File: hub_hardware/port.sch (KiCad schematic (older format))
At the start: 13 parts, among them P1 CONN_4, U4 ISL83485IBZ, U5 2CH-TVS

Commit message: kicad hardware files
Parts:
- C7: value C -> 100n; footprint ~ -> SA0603
- D3, D4: footprint (none) -> SA0603_LED
- P1: footprint (none) -> Assman-6p4c
- R10: footprint (none) -> C2
- R11: value 2K2 -> 10K; footprint (none) -> SA0603
- R43, R6, R7, R8, R9: footprint (none) -> SA0603
- U4: footprint (none) -> SO8E
- U5: footprint (none) -> SOT23
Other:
- note added: "PTC optional"

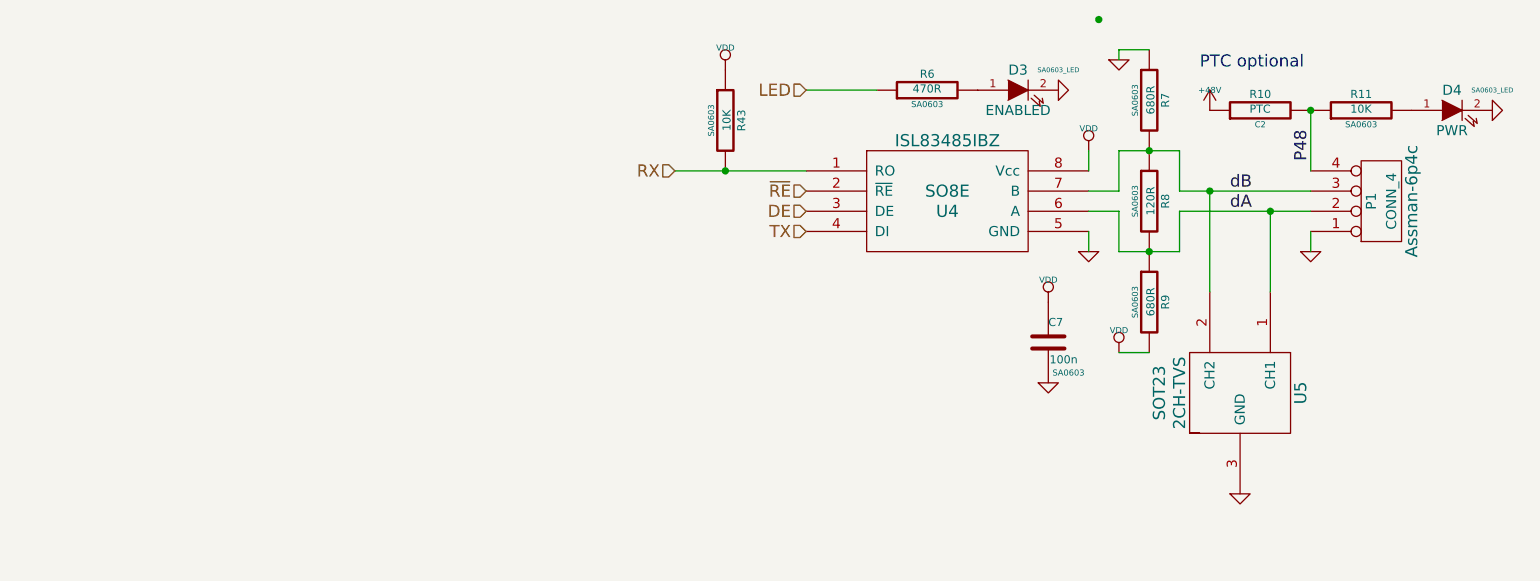
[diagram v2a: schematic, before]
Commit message: Copper for the hub
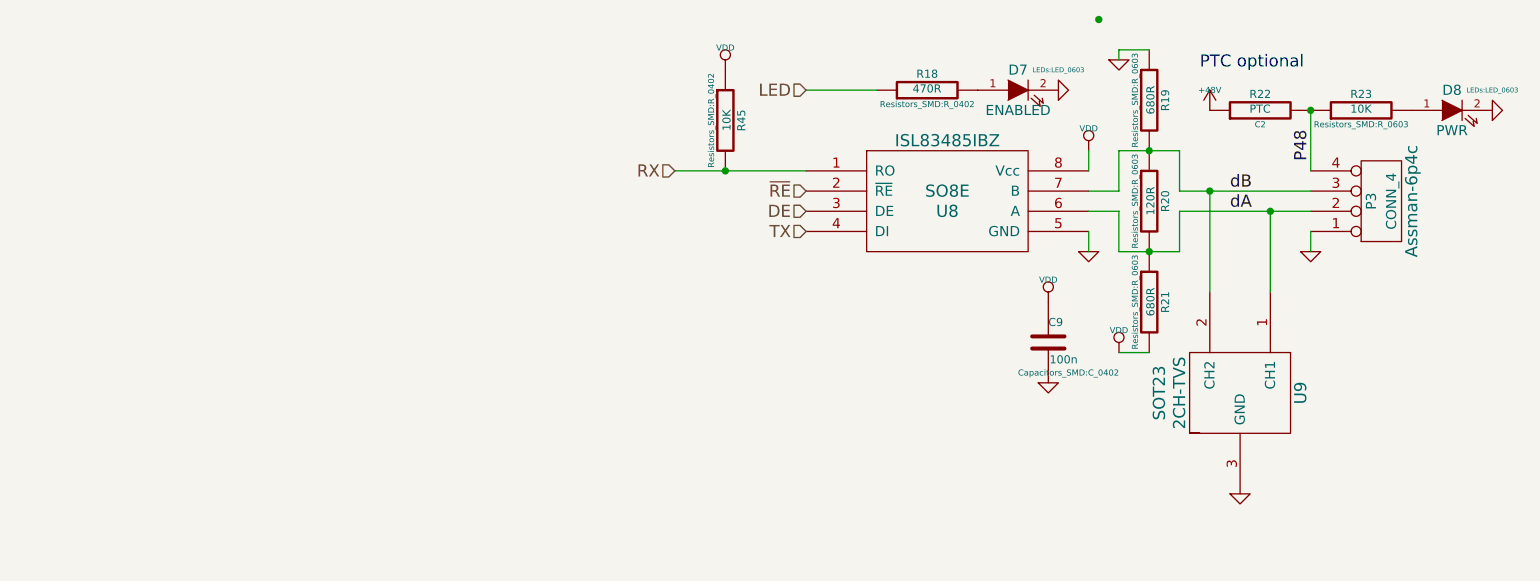
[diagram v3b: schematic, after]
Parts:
- C7: footprint SA0603 -> Capacitors_SMD:C_0402
- D3, D4: footprint SA0603_LED -> LEDs:LED_0603
- R11, R7, R8, R9: footprint SA0603 -> Resistors_SMD:R_0603
- R43, R6: footprint SA0603 -> Resistors_SMD:R_0402
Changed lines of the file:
@@
 AR Path="/556BE805/556BC9D7" Ref="P5"  Part="1"
 AR Path="/556BE816/556BC9D7" Ref="P6"  Part="1"
-F 0 "P1" V 7700 3700 50  0000 C CNN
+F 0 "P3" V 7700 3700 50  0000 C CNN
 F 1 "CONN_4" V 7800 3700 50  0000 C CNN
 F 2 "Assman-6p4c" V 7900 3700 60  0000 C CNN
@@
 AR Path="/556BE816/556BC9DD" Ref="R38"  Part="1"
 AR Path="/556BC9DD" Ref="R38"  Part="1"
-F 0 "R8" V 6680 3700 40  0000 C CNN
+F 0 "R20" V 6680 3700 40  0000 C CNN
 F 1 "120R" V 6607 3701 40  0000 C CNN
-F 2 "SA0603" V 6530 3700 30  0000 C CNN
+F 2 "Resistors_SMD:R_0603" V 6530 3700 30  0000 C CNN
 F 3 "" H 6600 3700 30  0000 C CNN
 	1    6600 3700
@@
 AR Path="/556BE805/556BC9EF" Ref="U12"  Part="1"
 AR Path="/556BE816/556BC9EF" Ref="U14"  Part="1"
-F 0 "U4" H 5600 3650 60  0000 C CNN
+F 0 "U8" H 5600 3650 60  0000 C CNN
 F 1 "ISL83485IBZ" H 5600 4000 60  0000 C CNN
 F 2 "SO8E" H 5600 3750 60  0000 C CNN
@@
 AR Path="/556BE805/556BCB2D" Ref="U13"  Part="1"
 AR Path="/556BE816/556BCB2D" Ref="U15"  Part="1"
-F 0 "U5" H 7050 4950 60  0000 C CNN
+F 0 "U9" H 7050 4950 60  0000 C CNN
 F 1 "2CH-TVS" H 7050 4350 60  0000 C CNN
 F 2 "SOT23" H 7050 4250 60  0000 C CNN
@@
 AR Path="/556BE816/556BCC86" Ref="R40"  Part="1"
 AR Path="/556BCC86" Ref="R40"  Part="1"
-F 0 "R10" V 7230 3250 40  0000 C CNN
+F 0 "R22" V 7230 3250 40  0000 C CNN
 F 1 "PTC" V 7157 3251 40  0000 C CNN
 F 2 "C2" V 7080 3250 30  0000 C CNN
@@
 AR Path="/556BE816/556BCD66" Ref="R41"  Part="1"
 AR Path="/556BCD66" Ref="R41"  Part="1"
-F 0 "R11" V 7730 3250 40  0000 C CNN
+F 0 "R23" V 7730 3250 40  0000 C CNN
 F 1 "10K" V 7657 3251 40  0000 C CNN
-F 2 "SA0603" V 7580 3250 30  0000 C CNN
+F 2 "Resistors_SMD:R_0603" V 7580 3250 30  0000 C CNN
 F 3 "" H 7650 3250 30  0000 C CNN
 	1    7650 3250
@@
 AR Path="/556BE816/556BCD84" Ref="D14"  Part="1"
 AR Path="/556BCD84" Ref="D14"  Part="1"
-F 0 "D4" H 8100 3350 50  0000 C CNN
+F 0 "D8" H 8100 3350 50  0000 C CNN
 F 1 "PWR" H 8100 3150 50  0000 C CNN
-F 2 "SA0603_LED" H 8300 3350 24  0000 C CNN
+F 2 "LEDs:LED_0603" H 8300 3350 24  0000 C CNN
 F 3 "" H 8100 3250 60  0000 C CNN
 	1    8100 3250
@@
 AR Path="/556BE816/556BCEEE" Ref="R36"  Part="1"
 AR Path="/556BCEEE" Ref="R36"  Part="1"
-F 0 "R6" V 5580 3150 40  0000 C CNN
+F 0 "R18" V 5580 3150 40  0000 C CNN
 F 1 "470R" V 5507 3151 40  0000 C CNN
-F 2 "SA0603" V 5430 3150 30  0000 C CNN
+F 2 "Resistors_SMD:R_0402" V 5430 3150 30  0000 C CNN
 F 3 "" H 5500 3150 30  0000 C CNN
 	1    5500 3150
@@
 AR Path="/556BE816/556BCEFD" Ref="D13"  Part="1"
 AR Path="/556BCEFD" Ref="D13"  Part="1"
-F 0 "D3" H 5950 3250 50  0000 C CNN
+F 0 "D7" H 5950 3250 50  0000 C CNN
 F 1 "ENABLED" H 5950 3050 50  0000 C CNN
-F 2 "SA0603_LED" H 6150 3250 24  0000 C CNN
+F 2 "LEDs:LED_0603" H 6150 3250 24  0000 C CNN
 F 3 "" H 5950 3150 60  0000 C CNN
 	1    5950 3150
@@
 AR Path="/556BE816/556BD0FA" Ref="R39"  Part="1"
 AR Path="/556BD0FA" Ref="R39"  Part="1"
-F 0 "R9" V 6680 4200 40  0000 C CNN
+F 0 "R21" V 6680 4200 40  0000 C CNN
 F 1 "680R" V 6607 4201 40  0000 C CNN
-F 2 "SA0603" V 6530 4200 30  0000 C CNN
+F 2 "Resistors_SMD:R_0603" V 6530 4200 30  0000 C CNN
 F 3 "" H 6600 4200 30  0000 C CNN
 	1    6600 4200
@@
 AR Path="/556BE816/556BD4F2" Ref="R37"  Part="1"
 AR Path="/556BD4F2" Ref="R37"  Part="1"
-F 0 "R7" V 6680 3200 40  0000 C CNN
+F 0 "R19" V 6680 3200 40  0000 C CNN
 F 1 "680R" V 6607 3201 40  0000 C CNN
-F 2 "SA0603" V 6530 3200 30  0000 C CNN
+F 2 "Resistors_SMD:R_0603" V 6530 3200 30  0000 C CNN
 F 3 "" H 6600 3200 30  0000 C CNN
 	1    6600 3200
@@
 AR Path="/556BE816/556BE2B4" Ref="R48"  Part="1"
 AR Path="/556BE2B4" Ref="R48"  Part="1"
-F 0 "R43" V 4580 3300 40  0000 C CNN
+F 0 "R45" V 4580 3300 40  0000 C CNN
 F 1 "10K" V 4507 3301 40  0000 C CNN
-F 2 "SA0603" V 4430 3300 30  0000 C CNN
+F 2 "Resistors_SMD:R_0402" V 4430 3300 30  0000 C CNN
 F 3 "" H 4500 3300 30  0000 C CNN
 	1    4500 3300
@@
 AR Path="/556BE816/556C536A" Ref="C12"  Part="1"
 AR Path="/556C536A" Ref="C12"  Part="1"
-F 0 "C7" H 6100 4500 40  0000 L CNN
+F 0 "C9" H 6100 4500 40  0000 L CNN
 F 1 "100n" H 6106 4315 40  0000 L CNN
-F 2 "SA0603" H 6200 4250 30  0000 C CNN
+F 2 "Capacitors_SMD:C_0402" H 6200 4250 30  0000 C CNN
 F 3 "~" H 6100 4400 60  0000 C CNN
 	1    6100 4400

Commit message: Hub gerbers; Reverting changes to lux API;
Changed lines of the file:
@@
 AR Path="/556BE805/556BC9D7" Ref="P5"  Part="1"
 AR Path="/556BE816/556BC9D7" Ref="P6"  Part="1"
-F 0 "P3" V 7700 3700 50  0000 C CNN
+F 0 "P1" V 7700 3700 50  0000 C CNN
 F 1 "CONN_4" V 7800 3700 50  0000 C CNN
 F 2 "Assman-6p4c" V 7900 3700 60  0000 C CNN
@@
 AR Path="/556BE816/556BC9DD" Ref="R38"  Part="1"
 AR Path="/556BC9DD" Ref="R38"  Part="1"
-F 0 "R20" V 6680 3700 40  0000 C CNN
+F 0 "R8" V 6680 3700 40  0000 C CNN
 F 1 "120R" V 6607 3701 40  0000 C CNN
 F 2 "Resistors_SMD:R_0603" V 6530 3700 30  0000 C CNN
@@
 AR Path="/556BE816/556BC9E3" Ref="#PWR099"  Part="1"
 AR Path="/556BC9E3" Ref="#PWR098"  Part="1"
-F 0 "#PWR099" H 7400 3950 30  0001 C CNN
+F 0 "#PWR039" H 7400 3950 30  0001 C CNN
 F 1 "GND" H 7400 3880 30  0001 C CNN
 F 2 "" H 7400 3950 60  0000 C CNN
@@
 AR Path="/556BE805/556BC9E9" Ref="#PWR088"  Part="1"
 AR Path="/556BE816/556BC9E9" Ref="#PWR0100"  Part="1"
-F 0 "#PWR0100" H 6900 3380 20  0001 C CNN
+F 0 "#PWR040" H 6900 3380 20  0001 C CNN
 F 1 "+48V" H 6900 3350 30  0000 C CNN
 F 2 "" H 6900 3250 60  0000 C CNN
@@
 AR Path="/556BE805/556BC9EF" Ref="U12"  Part="1"
 AR Path="/556BE816/556BC9EF" Ref="U14"  Part="1"
-F 0 "U8" H 5600 3650 60  0000 C CNN
+F 0 "U4" H 5600 3650 60  0000 C CNN
 F 1 "ISL83485IBZ" H 5600 4000 60  0000 C CNN
 F 2 "SO8E" H 5600 3750 60  0000 C CNN
@@
 AR Path="/556BE816/556BC9F5" Ref="#PWR0101"  Part="1"
 AR Path="/556BC9F5" Ref="#PWR0100"  Part="1"
-F 0 "#PWR0101" H 6300 3950 30  0001 C CNN
+F 0 "#PWR041" H 6300 3950 30  0001 C CNN
 F 1 "GND" H 6300 3880 30  0001 C CNN
 F 2 "" H 6300 3950 60  0000 C CNN
@@
 AR Path="/556BE805/556BCABF" Ref="#PWR090"  Part="1"
 AR Path="/556BE816/556BCABF" Ref="#PWR0102"  Part="1"
-F 0 "#PWR0102" H 6300 3550 30  0001 C CNN
+F 0 "#PWR042" H 6300 3550 30  0001 C CNN
 F 1 "VDD" H 6300 3560 30  0000 C CNN
 F 2 "" H 6300 3450 60  0000 C CNN
@@
 AR Path="/556BE805/556BCB2D" Ref="U13"  Part="1"
 AR Path="/556BE816/556BCB2D" Ref="U15"  Part="1"
-F 0 "U9" H 7050 4950 60  0000 C CNN
+F 0 "U5" H 7050 4950 60  0000 C CNN
 F 1 "2CH-TVS" H 7050 4350 60  0000 C CNN
 F 2 "SOT23" H 7050 4250 60  0000 C CNN
@@
 AR Path="/556BE816/556BCC19" Ref="#PWR0103"  Part="1"
 AR Path="/556BCC19" Ref="#PWR0102"  Part="1"
-F 0 "#PWR0103" H 7050 5150 30  0001 C CNN
+F 0 "#PWR043" H 7050 5150 30  0001 C CNN
 F 1 "GND" H 7050 5080 30  0001 C CNN
 F 2 "" H 7050 5150 60  0000 C CNN
@@
 AR Path="/556BE816/556BCC86" Ref="R40"  Part="1"
 AR Path="/556BCC86" Ref="R40"  Part="1"
-F 0 "R22" V 7230 3250 40  0000 C CNN
+F 0 "R10" V 7230 3250 40  0000 C CNN
 F 1 "PTC" V 7157 3251 40  0000 C CNN
 F 2 "C2" V 7080 3250 30  0000 C CNN
@@
 AR Path="/556BE816/556BCD66" Ref="R41"  Part="1"
 AR Path="/556BCD66" Ref="R41"  Part="1"
-F 0 "R23" V 7730 3250 40  0000 C CNN
+F 0 "R11" V 7730 3250 40  0000 C CNN
 F 1 "10K" V 7657 3251 40  0000 C CNN
 F 2 "Resistors_SMD:R_0603" V 7580 3250 30  0000 C CNN
@@
 AR Path="/556BE816/556BCD84" Ref="D14"  Part="1"
 AR Path="/556BCD84" Ref="D14"  Part="1"
-F 0 "D8" H 8100 3350 50  0000 C CNN
+F 0 "D4" H 8100 3350 50  0000 C CNN
 F 1 "PWR" H 8100 3150 50  0000 C CNN
 F 2 "LEDs:LED_0603" H 8300 3350 24  0000 C CNN
@@
 AR Path="/556BE816/556BCD93" Ref="#PWR0104"  Part="1"
 AR Path="/556BCD93" Ref="#PWR0103"  Part="1"
-F 0 "#PWR0104" H 8300 3250 30  0001 C CNN
+F 0 "#PWR044" H 8300 3250 30  0001 C CNN
 F 1 "GND" H 8300 3180 30  0001 C CNN
 F 2 "" H 8300 3250 60  0000 C CNN
@@
 AR Path="/556BE816/556BCEEE" Ref="R36"  Part="1"
 AR Path="/556BCEEE" Ref="R36"  Part="1"
-F 0 "R18" V 5580 3150 40  0000 C CNN
+F 0 "R6" V 5580 3150 40  0000 C CNN
 F 1 "470R" V 5507 3151 40  0000 C CNN
 F 2 "Resistors_SMD:R_0402" V 5430 3150 30  0000 C CNN
@@
 AR Path="/556BE816/556BCEFD" Ref="D13"  Part="1"
 AR Path="/556BCEFD" Ref="D13"  Part="1"
-F 0 "D7" H 5950 3250 50  0000 C CNN
+F 0 "D3" H 5950 3250 50  0000 C CNN
 F 1 "ENABLED" H 5950 3050 50  0000 C CNN
 F 2 "LEDs:LED_0603" H 6150 3250 24  0000 C CNN
@@
 AR Path="/556BE816/556BCF0C" Ref="#PWR0105"  Part="1"
 AR Path="/556BCF0C" Ref="#PWR0104"  Part="1"
-F 0 "#PWR0105" H 6150 3150 30  0001 C CNN
+F 0 "#PWR045" H 6150 3150 30  0001 C CNN
 F 1 "GND" H 6150 3080 30  0001 C CNN
 F 2 "" H 6150 3150 60  0000 C CNN
@@
 AR Path="/556BE816/556BD0FA" Ref="R39"  Part="1"
 AR Path="/556BD0FA" Ref="R39"  Part="1"
-F 0 "R21" V 6680 4200 40  0000 C CNN
+F 0 "R9" V 6680 4200 40  0000 C CNN
 F 1 "680R" V 6607 4201 40  0000 C CNN
 F 2 "Resistors_SMD:R_0603" V 6530 4200 30  0000 C CNN
@@
 AR Path="/556BE805/556BD10E" Ref="#PWR094"  Part="1"
 AR Path="/556BE816/556BD10E" Ref="#PWR0106"  Part="1"
-F 0 "#PWR0106" H 6450 4550 30  0001 C CNN
+F 0 "#PWR046" H 6450 4550 30  0001 C CNN
 F 1 "VDD" H 6450 4560 30  0000 C CNN
 F 2 "" H 6450 4450 60  0000 C CNN
@@
 AR Path="/556BE816/556BD4F2" Ref="R37"  Part="1"
 AR Path="/556BD4F2" Ref="R37"  Part="1"
-F 0 "R19" V 6680 3200 40  0000 C CNN
+F 0 "R7" V 6680 3200 40  0000 C CNN
 F 1 "680R" V 6607 3201 40  0000 C CNN
 F 2 "Resistors_SMD:R_0603" V 6530 3200 30  0000 C CNN
@@
 AR Path="/556BE816/556BD523" Ref="#PWR0107"  Part="1"
 AR Path="/556BD523" Ref="#PWR0106"  Part="1"
-F 0 "#PWR0107" H 6450 3000 30  0001 C CNN
+F 0 "#PWR047" H 6450 3000 30  0001 C CNN
 F 1 "GND" H 6450 2930 30  0001 C CNN
 F 2 "" H 6450 3000 60  0000 C CNN
@@
 AR Path="/556BE816/556BE2B4" Ref="R48"  Part="1"
 AR Path="/556BE2B4" Ref="R48"  Part="1"
-F 0 "R45" V 4580 3300 40  0000 C CNN
+F 0 "R43" V 4580 3300 40  0000 C CNN
 F 1 "10K" V 4507 3301 40  0000 C CNN
 F 2 "Resistors_SMD:R_0402" V 4430 3300 30  0000 C CNN
@@
 AR Path="/556BE805/556BE2DD" Ref="#PWR096"  Part="1"
 AR Path="/556BE816/556BE2DD" Ref="#PWR0108"  Part="1"
-F 0 "#PWR0108" H 4500 3150 30  0001 C CNN
+F 0 "#PWR048" H 4500 3150 30  0001 C CNN
 F 1 "VDD" H 4500 3160 30  0000 C CNN
 F 2 "" H 4500 3050 60  0000 C CNN
@@
 AR Path="/556BE805/556C535C" Ref="#PWR097"  Part="1"
 AR Path="/556BE816/556C535C" Ref="#PWR0109"  Part="1"
-F 0 "#PWR0109" H 6100 4300 30  0001 C CNN
+F 0 "#PWR049" H 6100 4300 30  0001 C CNN
 F 1 "VDD" H 6100 4310 30  0000 C CNN
 F 2 "" H 6100 4200 60  0000 C CNN
@@
 AR Path="/556BE816/556C5362" Ref="#PWR0110"  Part="1"
 AR Path="/556C5362" Ref="#PWR0109"  Part="1"
-F 0 "#PWR0110" H 6100 4600 30  0001 C CNN
+F 0 "#PWR050" H 6100 4600 30  0001 C CNN
 F 1 "GND" H 6100 4530 30  0001 C CNN
 F 2 "" H 6100 4600 60  0000 C CNN
@@
 AR Path="/556BE816/556C536A" Ref="C12"  Part="1"
 AR Path="/556C536A" Ref="C12"  Part="1"
-F 0 "C9" H 6100 4500 40  0000 L CNN
+F 0 "C7" H 6100 4500 40  0000 L CNN
 F 1 "100n" H 6106 4315 40  0000 L CNN
 F 2 "Capacitors_SMD:C_0402" H 6200 4250 30  0000 C CNN
@@
 PTC optional
 Connection ~ 6350 2800
+Connection ~ 5800 3950
 $EndSCHEMATC

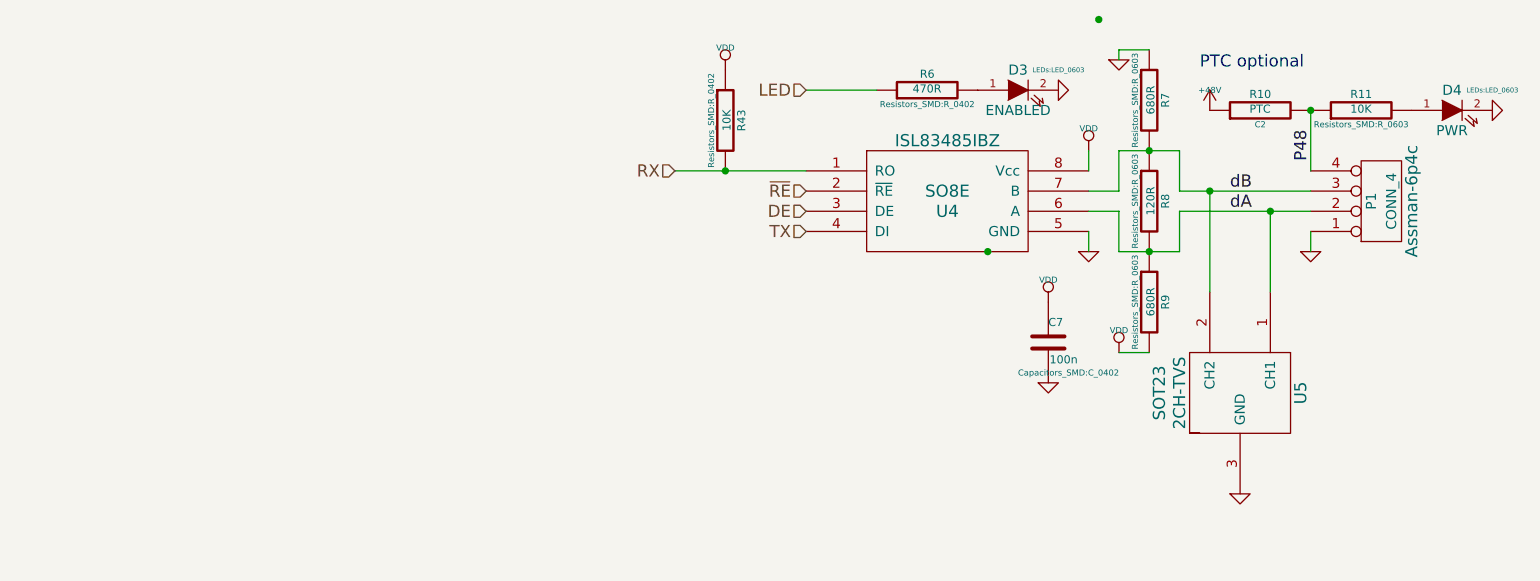
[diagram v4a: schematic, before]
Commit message: WIP Lux Hub v7
* Replace PTCs with current-limiting circuit
* Widen board and add 4x2mm mounting holes
* TODO: Rearrange some components on the edges
* TODO: Check silkscreen (esp. LEDs)
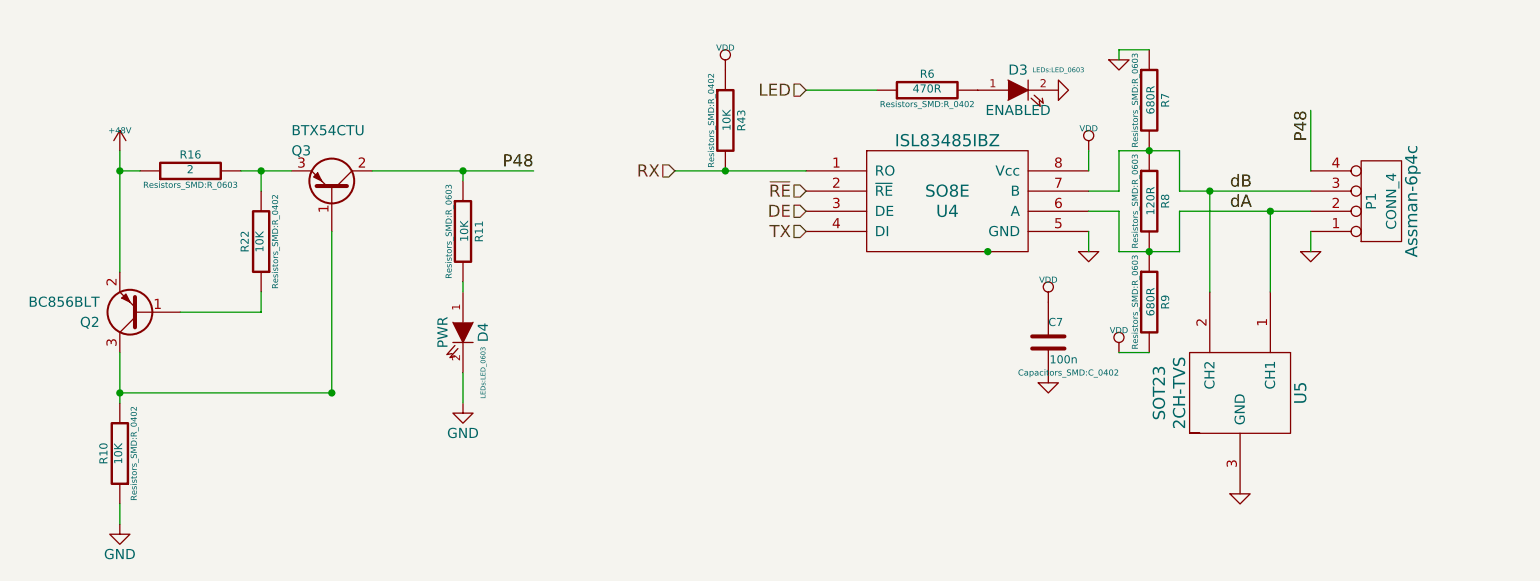
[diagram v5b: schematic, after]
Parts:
- added Q2: BC856BLT, TO_SOT_Packages_THT:TO-220-3_Vertical, symbol BC856
- added Q3: BTX54CTU, TO_SOT_Packages_SMD:SOT-23, symbol Q_PNP_BCE
- added R16: 2, Resistors_SMD:R_0603, symbol R-RESCUE-lux_hub
- added R22: 10K, Resistors_SMD:R_0402, symbol R-RESCUE-lux_hub
- R10: value PTC -> 10K; footprint C2 -> Resistors_SMD:R_0402
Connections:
- net +48V: now also Q2.2 (E), R16.1; no longer R10.1
- net GND: now also R10.1
- net P48: now also Q3.2 (C); no longer R10.2
- new net: Q2.3 (C), Q3.1 (B), R10.2
- new net: Q2.1 (B), R22.1
- new net: Q3.3 (E), R16.2, R22.2
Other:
- note removed: "PTC optional"
- moved on the sheet: D4, R11

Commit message: Lux Hub v8
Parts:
- removed D3: ENABLED, LEDs:LED_0603, symbol LED-RESCUE-lux_hub
- removed Q2: BC856BLT, TO_SOT_Packages_THT:TO-220-3_Vertical, symbol BC856
- removed Q3: BTX54CTU, TO_SOT_Packages_SMD:SOT-23, symbol Q_PNP_BCE
- removed R10, R22: 10K, Resistors_SMD:R_0402, symbol R-RESCUE-lux_hub
- removed R16: 2, Resistors_SMD:R_0603, symbol R-RESCUE-lux_hub
- removed R6: 470R, Resistors_SMD:R_0402, symbol R-RESCUE-lux_hub
- added U16: BTS4175SGA, SMD_Packages:SOIC-8-N, symbol BTS4175SGA
- C7: footprint Capacitors_SMD:C_0402 -> Capacitors_SMD:C_0603
- R43: footprint Resistors_SMD:R_0402 -> Resistors_SMD:R_0603
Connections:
- net +48V: now also U16.5 (VS), U16.6 (VS), U16.7 (VS), U16.8 (VS)
- net GND: now also U16.1 (GND)
- net P48: now also U16.3 (OUT)
- new net PWR_EN: U16.2 (IN)
- no-connect marks 0 -> 1
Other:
- moved on the sheet: D14, R41
